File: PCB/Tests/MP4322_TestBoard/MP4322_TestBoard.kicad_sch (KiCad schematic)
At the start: 0 parts

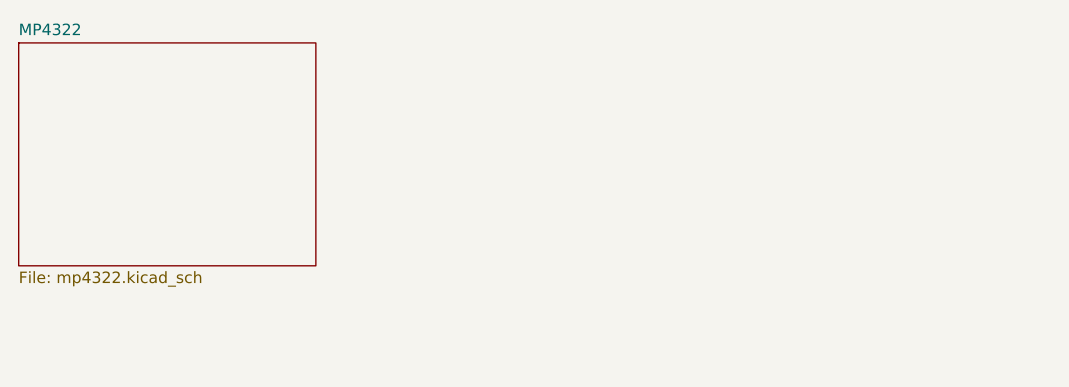
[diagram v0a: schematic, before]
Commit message: Finished MP4322 evaluation board
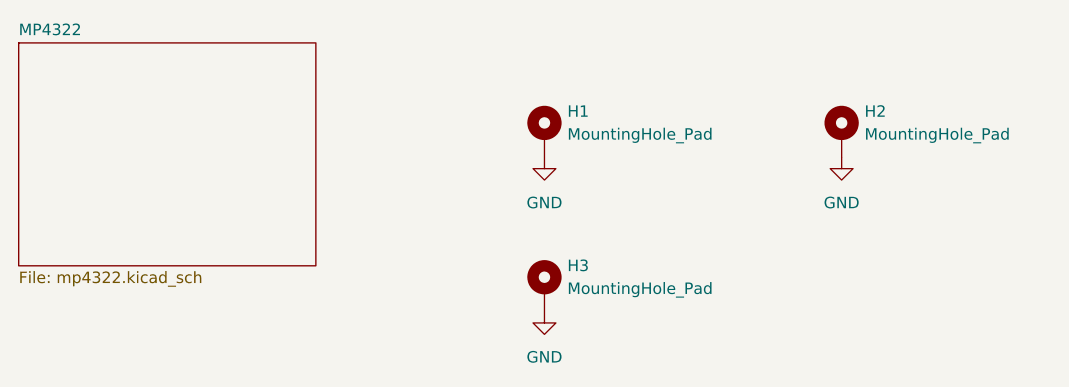
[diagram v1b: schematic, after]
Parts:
- added H1, H2, H3: MountingHole_Pad, MountingHole:MountingHole_2.2mm_M2_ISO7380_Pad_TopBottom, symbol Mechanical:MountingHole_Pad
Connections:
- new net GND: H1.1, H2.1, H3.1
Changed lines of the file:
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@@
 (kicad_sch (version 20211123) (generator eeschema)
   (paper "A4")
+  (symbol (lib_id "power:GND") (at 146.05 100.965 0) (unit 1)
+    (in_bom yes) (on_board yes) (fields_autoplaced)
+    (property "Reference" "#PWR0114" (id 0) (at 146.05 107.315 0)
+      (effects (font (size 1.27 1.27)) hide)
+    )
+    (property "Value" "GND" (id 1) (at 146.05 106.045 0))
+    (property "Footprint" "" (id 2) (at 146.05 100.965 0)
+      (effects (font (size 1.27 1.27)) hide)
+    )
+    (property "Datasheet" "" (id 3) (at 146.05 100.965 0)
+      (effects (font (size 1.27 1.27)) hide)
+    )
+    (pin "1")
+  )
+  (symbol (lib_id "power:GND") (at 179.07 83.82 0) (unit 1)
+    (in_bom yes) (on_board yes) (fields_autoplaced)
+    (property "Reference" "#PWR0113" (id 0) (at 179.07 90.17 0)
+      (effects (font (size 1.27 1.27)) hide)
+    )
+    (property "Value" "GND" (id 1) (at 179.07 88.9 0))
+    (property "Footprint" "" (id 2) (at 179.07 83.82 0)
+      (effects (font (size 1.27 1.27)) hide)
+    )
+    (property "Datasheet" "" (id 3) (at 179.07 83.82 0)
+      (effects (font (size 1.27 1.27)) hide)
+    )
+    (pin "1")
+  )
+  (symbol (lib_id "Mechanical:MountingHole_Pad") (at 146.05 98.425 0) (unit 1)
+    (in_bom yes) (on_board yes) (fields_autoplaced)
+    (property "Reference" "H3" (id 0) (at 148.59 95.8849 0)
+      (effects (font (size 1.27 1.27)) (justify left))
+    )
+    (property "Value" "MountingHole_Pad" (id 1) (at 148.59 98.4249 0)
+      (effects (font (size 1.27 1.27)) (justify left))
+    )
+    (property "Footprint" "MountingHole:MountingHole_2.2mm_M2_ISO7380_Pad_TopBottom" (id 2) (at 146.05 98.425 0)
+      (effects (font (size 1.27 1.27)) hide)
+    )
+    (property "Datasheet" "~" (id 3) (at 146.05 98.425 0)
+      (effects (font (size 1.27 1.27)) hide)
+    )
+    (pin "1")
+  )
+  (symbol (lib_id "Mechanical:MountingHole_Pad") (at 146.05 81.28 0) (unit 1)
+    (in_bom yes) (on_board yes) (fields_autoplaced)
+    (property "Reference" "H1" (id 0) (at 148.59 78.7399 0)
+      (effects (font (size 1.27 1.27)) (justify left))
+    )
+    (property "Value" "MountingHole_Pad" (id 1) (at 148.59 81.2799 0)
+      (effects (font (size 1.27 1.27)) (justify left))
+    )
+    (property "Footprint" "MountingHole:MountingHole_2.2mm_M2_ISO7380_Pad_TopBottom" (id 2) (at 146.05 81.28 0)
+      (effects (font (size 1.27 1.27)) hide)
+    )
+    (property "Datasheet" "~" (id 3) (at 146.05 81.28 0)
+      (effects (font (size 1.27 1.27)) hide)
+    )
+    (pin "1")
+  )
+  (symbol (lib_id "Mechanical:MountingHole_Pad") (at 179.07 81.28 0) (unit 1)
+    (in_bom yes) (on_board yes) (fields_autoplaced)
+    (property "Reference" "H2" (id 0) (at 181.61 78.7399 0)
+      (effects (font (size 1.27 1.27)) (justify left))
+    )
+    (property "Value" "MountingHole_Pad" (id 1) (at 181.61 81.2799 0)
+      (effects (font (size 1.27 1.27)) (justify left))
+    )
+    (property "Footprint" "MountingHole:MountingHole_2.2mm_M2_ISO7380_Pad_TopBottom" (id 2) (at 179.07 81.28 0)
+      (effects (font (size 1.27 1.27)) hide)
+    )
+    (property "Datasheet" "~" (id 3) (at 179.07 81.28 0)
+      (effects (font (size 1.27 1.27)) hide)
+    )
+    (pin "1")
+  )
+  (symbol (lib_id "power:GND") (at 146.05 83.82 0) (unit 1)
+    (in_bom yes) (on_board yes) (fields_autoplaced)
+    (property "Reference" "#PWR0112" (id 0) (at 146.05 90.17 0)
+      (effects (font (size 1.27 1.27)) hide)
+    )
+    (property "Value" "GND" (id 1) (at 146.05 88.9 0))
+    (property "Footprint" "" (id 2) (at 146.05 83.82 0)
+      (effects (font (size 1.27 1.27)) hide)
+    )
+    (property "Datasheet" "" (id 3) (at 146.05 83.82 0)
+      (effects (font (size 1.27 1.27)) hide)
+    )
+    (pin "1")
+  )
   (sheet (at 87.63 71.12) (size 33.02 24.765) (fields_autoplaced)
     (stroke (width 0.1524) (type solid) (color 0 0 0 0))
@@
       (reference "#PWR0111") (unit 1) (value "GND") (footprint "")
     )
+    (path "/fe2e34d0-c124-4bfb-a35f-f5829b22f8e8"
+      (reference "#PWR0112") (unit 1) (value "GND") (footprint "")
+    )
+    (path "/b38917ff-505d-4c68-90ad-f405c0b9dc4f"
+      (reference "#PWR0113") (unit 1) (value "GND") (footprint "")
+    )
+    (path "/6bdd24c6-3401-40b5-84d4-d703e2e0d096"
+      (reference "#PWR0114") (unit 1) (value "GND") (footprint "")
+    )
     (path "/15f8ef37-b8ff-46af-97c5-8082b5f7e685/04c86f84-a680-4050-a69a-6b9f4cb58bab"
       (reference "#PWR0192") (unit 1) (value "GND") (footprint "")
@@
     )
     (path "/15f8ef37-b8ff-46af-97c5-8082b5f7e685/09110563-b95e-40cd-a3de-641b81fcbefd"
-      (reference "C1") (unit 1) (value "1nF") (footprint "Resistor_SMD:R_0402_1005Metric")
+      (reference "C1") (unit 1) (value "1nF") (footprint "Capacitor_SMD:C_0402_1005Metric")
     )
     (path "/15f8ef37-b8ff-46af-97c5-8082b5f7e685/518a795f-1252-4eb3-a667-0ba655385d8e"
-      (reference "C2") (unit 1) (value "10nF") (footprint "Resistor_SMD:R_0402_1005Metric")
+      (reference "C2") (unit 1) (value "10nF") (footprint "Capacitor_SMD:C_0402_1005Metric")
     )
     (path "/15f8ef37-b8ff-46af-97c5-8082b5f7e685/bc427b19-37fa-4075-b9fc-b75ca55c4121"
@@
     )
     (path "/15f8ef37-b8ff-46af-97c5-8082b5f7e685/c7a400ff-ba65-4f1d-8d61-9921ea157c67"
-      (reference "C27") (unit 1) (value "1uF") (footprint "Resistor_SMD:R_0402_1005Metric")
+      (reference "C27") (unit 1) (value "1uF") (footprint "Capacitor_SMD:C_0402_1005Metric")
     )
     (path "/15f8ef37-b8ff-46af-97c5-8082b5f7e685/f22d2272-7682-4097-8e61-e570a7ba5672"
-      (reference "C28") (unit 1) (value "47nF") (footprint "Resistor_SMD:R_0402_1005Metric")
+      (reference "C28") (unit 1) (value "47nF") (footprint "Capacitor_SMD:C_0402_1005Metric")
     )
     (path "/15f8ef37-b8ff-46af-97c5-8082b5f7e685/ff09350d-fa69-4e74-9951-fc69dcd4fd6d"
-      (reference "C29") (unit 1) (value "10pF") (footprint "Resistor_SMD:R_0402_1005Metric")
+      (reference "C29") (unit 1) (value "10pF") (footprint "Capacitor_SMD:C_0402_1005Metric")
     )
     (path "/15f8ef37-b8ff-46af-97c5-8082b5f7e685/f0f6583c-7422-4f38-95f0-93c431d53722"
@@
     )
     (path "/15f8ef37-b8ff-46af-97c5-8082b5f7e685/21d58d35-fc72-4586-849f-899d2b3004c7"
-      (reference "F24") (unit 1) (value "500mA") (footprint "Fuse:Fuse_0805_2012Metric")
+      (reference "F24") (unit 1) (value "2A") (footprint "Fuse:Fuse_0805_2012Metric")
+    )
+    (path "/c350605b-5436-4844-a7af-b3f91ca0ff50"
+      (reference "H1") (unit 1) (value "MountingHole_Pad") (footprint "MountingHole:MountingHole_2.2mm_M2_ISO7380_Pad_TopBottom")
+    )
+    (path "/d938f1c2-868c-4d7e-8156-299b70707e83"
+      (reference "H2") (unit 1) (value "MountingHole_Pad") (footprint "MountingHole:MountingHole_2.2mm_M2_ISO7380_Pad_TopBottom")
+    )
+    (path "/be69efc2-f8a1-455f-b993-46df73a3e650"
+      (reference "H3") (unit 1) (value "MountingHole_Pad") (footprint "MountingHole:MountingHole_2.2mm_M2_ISO7380_Pad_TopBottom")
     )
     (path "/15f8ef37-b8ff-46af-97c5-8082b5f7e685/81fe675d-9767-4fb2-b2b8-3c57d0b3fa96"
